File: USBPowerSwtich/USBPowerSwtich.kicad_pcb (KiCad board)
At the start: 2 copper layers, 30.8 x 17 mm, 4 parts, among them J1 USB_A_Male, J2 USB_A_Female, J3 Test, SW1 Power

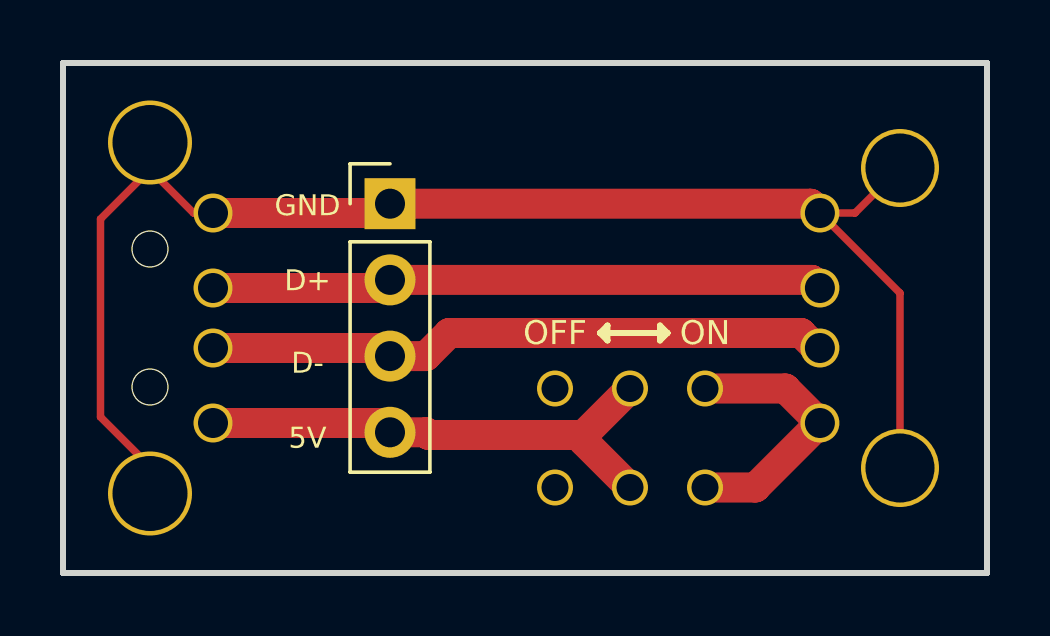
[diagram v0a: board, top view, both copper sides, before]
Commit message: Updating silkscreen and outline
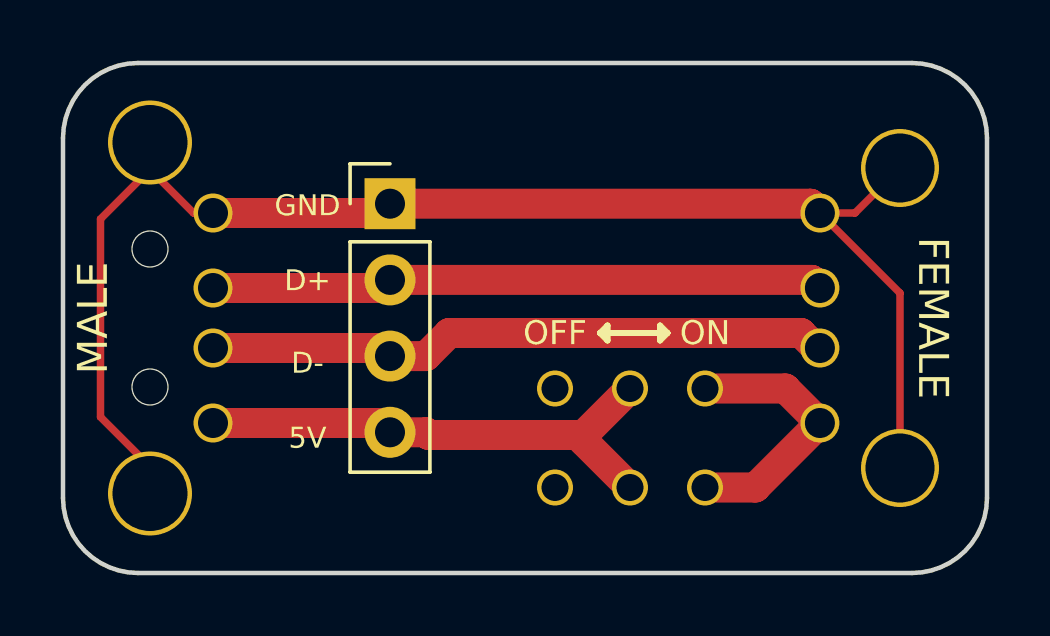
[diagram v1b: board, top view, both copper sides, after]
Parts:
- added G***: LOGO, Logos:logo_MLlabs_small, B.Cu at (87.2, 76.5)
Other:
- outline, holes or cut-outs redrawn
- board text added: "FEMALE"
- board text added: "MALE"
- board text added: "Maniacal Labs"

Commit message: Added name
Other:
- board text added: "USB Switch Buddy"
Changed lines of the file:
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@@
   (general
     (thickness 1.6)
-    (drawings 29)
+    (drawings 30)
     (tracks 38)
     (zones 0)
@@
       (xy 0.280132 4.064859)) (layer B.SilkS) (width 0.01))
   )
+  (gr_text "USB Switch Buddy" (at 78.6 87.3) (layer B.SilkS)
+    (effects (font (size 0.9 0.9) (thickness 0.225)) (justify mirror))
+  )
   (gr_text FEMALE (at 96.1 80 270) (layer F.SilkS)

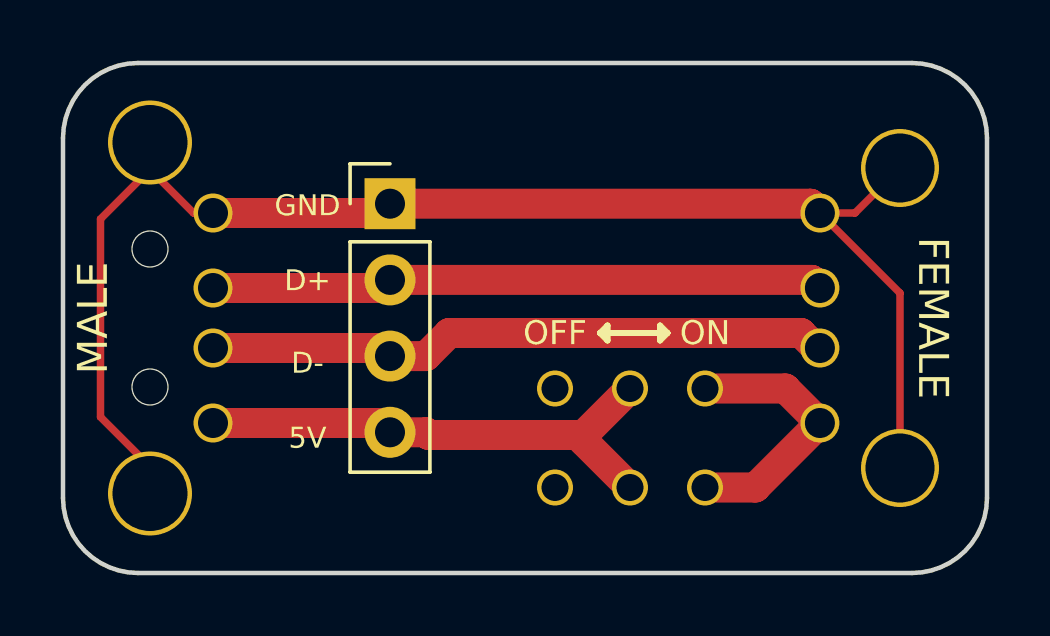
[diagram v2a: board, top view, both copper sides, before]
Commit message: Moving silk screen layout
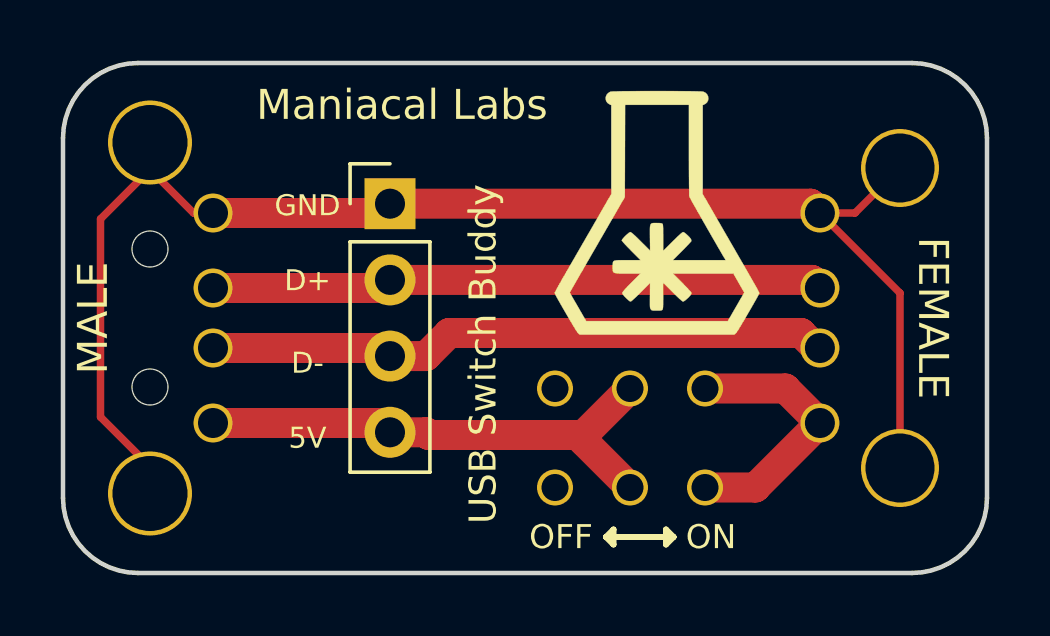
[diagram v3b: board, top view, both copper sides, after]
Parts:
- G***: moved to F.Cu
- moved G*** 0.35 mm to (86.9, 76.5), turned to 0 degrees

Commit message: Tweak switch placement
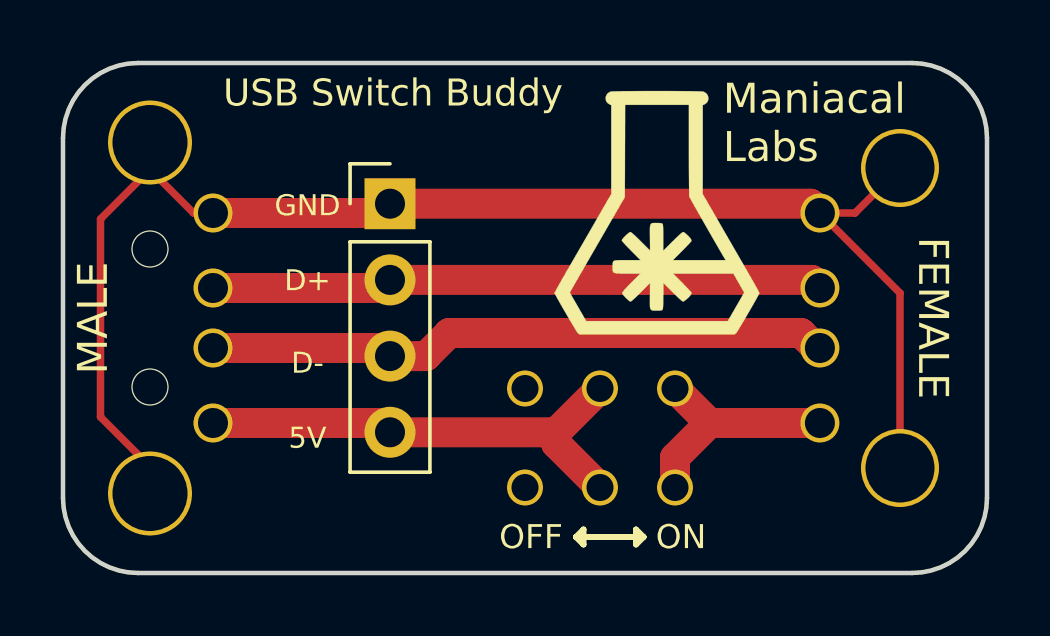
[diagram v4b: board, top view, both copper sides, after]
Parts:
- moved SW1 1.00 mm to (85.0, 84.0)
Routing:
- net Net-(J2-Pad1): track 9.03 -> 7.93 mm
- net VCC: track 17.1 -> 16.1 mm
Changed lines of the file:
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@@
     (thickness 1.6)
     (drawings 30)
-    (tracks 38)
+    (tracks 36)
     (zones 0)
     (modules 5)
@@
     (45 Margin user)
     (46 B.CrtYd user)
-    (47 F.CrtYd user)
+    (47 F.CrtYd user hide)
     (48 B.Fab user)
     (49 F.Fab user)
   )
   (setup
-    (last_trace_width 0.25)
+    (last_trace_width 1)
     (user_trace_width 1)
     (trace_clearance 0.2)
@@
     (aux_axis_origin 0 0)
     (grid_origin 67.1 88.5)
-    (visible_elements 7FFFFF7F)
+    (visible_elements 7FFFF77F)
     (pcbplotparams
       (layerselection 0x010fc_ffffffff)
@@
       (outputformat 1)
       (mirror false)
-      (drillshape 1)
+      (drillshape 0)
       (scaleselection 1)
-      (outputdirectory ""))
+      (outputdirectory "gerber/"))
   )
   (net 0 "")
@@
   )
   (module Custom:JS202011CQN (layer F.Cu)
-    (at 86 84)
+    (at 85 84)
     (descr https://www.mouser.com/datasheet/2/60/js-1382693.pdf)
     (fp_text reference SW1 (at 0 5) (layer F.SilkS) hide
@@
       (xy 0.280132 -4.064859)) (layer F.SilkS) (width 0.01))
   )
-  (gr_text "USB Switch Buddy" (at 81.1 81.2 90) (layer F.SilkS)
+  (gr_text "USB Switch Buddy" (at 78.1 72.5) (layer F.SilkS)
     (effects (font (size 0.9 0.9) (thickness 0.225)))
   )
@@
   (gr_arc (start 95.4 74) (end 97.9 74) (angle -90) (layer Edge.Cuts) (width 0.15))
   (gr_arc (start 69.6 74) (end 69.6 71.5) (angle -90) (layer Edge.Cuts) (width 0.15))
-  (gr_text "Maniacal Labs" (at 78.4 72.9) (layer F.SilkS)
-    (effects (font (size 1 1) (thickness 0.25)))
+  (gr_text "Maniacal\nLabs" (at 89.1 73.5) (layer F.SilkS)
+    (effects (font (size 1 1) (thickness 0.25)) (justify left))
   )
   (gr_text 5V (at 81 84) (layer B.SilkS)
@@
     (effects (font (size 0.7 0.7) (thickness 0.175)))
   )
-  (gr_line (start 85.45 87.55) (end 85.2 87.3) (layer F.SilkS) (width 0.2))
-  (gr_line (start 85.45 87.05) (end 85.45 87.55) (layer F.SilkS) (width 0.2))
-  (gr_line (start 85.2 87.3) (end 85.45 87.05) (layer F.SilkS) (width 0.2))
-  (gr_line (start 86.2 87.3) (end 85.2 87.3) (layer F.SilkS) (width 0.2))
-  (gr_line (start 87.2 87.55) (end 87.45 87.3) (layer F.SilkS) (width 0.2))
-  (gr_line (start 87.2 87.05) (end 87.2 87.55) (layer F.SilkS) (width 0.2))
-  (gr_line (start 87.45 87.3) (end 87.2 87.05) (layer F.SilkS) (width 0.2))
-  (gr_line (start 86.2 87.3) (end 87.45 87.3) (layer F.SilkS) (width 0.2))
-  (gr_text OFF (at 83.7 87.3) (layer F.SilkS)
+  (gr_line (start 84.45 87.55) (end 84.2 87.3) (layer F.SilkS) (width 0.2))
+  (gr_line (start 84.45 87.05) (end 84.45 87.55) (layer F.SilkS) (width 0.2))
+  (gr_line (start 84.2 87.3) (end 84.45 87.05) (layer F.SilkS) (width 0.2))
+  (gr_line (start 85.2 87.3) (end 84.2 87.3) (layer F.SilkS) (width 0.2))
+  (gr_line (start 86.2 87.55) (end 86.45 87.3) (layer F.SilkS) (width 0.2))
+  (gr_line (start 86.2 87.05) (end 86.2 87.55) (layer F.SilkS) (width 0.2))
+  (gr_line (start 86.45 87.3) (end 86.2 87.05) (layer F.SilkS) (width 0.2))
+  (gr_line (start 85.2 87.3) (end 86.45 87.3) (layer F.SilkS) (width 0.2))
+  (gr_text OFF (at 82.7 87.3) (layer F.SilkS)
     (effects (font (size 0.8 0.8) (thickness 0.2)))
   )
-  (gr_text ON (at 88.7 87.3) (layer F.SilkS)
+  (gr_text ON (at 87.7 87.3) (layer F.SilkS)
     (effects (font (size 0.8 0.8) (thickness 0.2)))
   )
@@
   (segment (start 77.69 83.5) (end 78 83.81) (width 1) (layer F.Cu) (net 2))
   (segment (start 72.1 83.5) (end 77.69 83.5) (width 1) (layer F.Cu) (net 2))
-  (segment (start 79.202081 83.81) (end 79.292081 83.9) (width 1) (layer F.Cu) (net 2))
-  (segment (start 78 83.81) (end 79.202081 83.81) (width 1) (layer F.Cu) (net 2))
-  (segment (start 84.45 83.9) (end 86 82.35) (width 1) (layer F.Cu) (net 2))
-  (segment (start 79.292081 83.9) (end 84.45 83.9) (width 1) (layer F.Cu) (net 2))
-  (segment (start 84.45 84.1) (end 86 85.65) (width 1) (layer F.Cu) (net 2))
-  (segment (start 84.45 83.9) (end 84.45 84.1) (width 1) (layer F.Cu) (net 2))
+  (segment (start 83.54 83.81) (end 85 82.35) (width 1) (layer F.Cu) (net 2))
+  (segment (start 78 83.81) (end 83.54 83.81) (width 1) (layer F.Cu) (net 2))
+  (segment (start 83.54 84.19) (end 85 85.65) (width 1) (layer F.Cu) (net 2))
+  (segment (start 83.54 83.81) (end 83.54 84.19) (width 1) (layer F.Cu) (net 2))
   (segment (start 77.73 81) (end 78 81.27) (width 1) (layer F.Cu) (net 3))
   (segment (start 72.1 81) (end 77.73 81) (width 1) (layer F.Cu) (net 3))
@@
   (segment (start 92.06 78.73) (end 92.33 79) (width 1) (layer F.Cu) (net 4))
   (segment (start 78 78.73) (end 92.06 78.73) (width 1) (layer F.Cu) (net 4))
-  (segment (start 91.18 82.35) (end 92.33 83.5) (width 1) (layer F.Cu) (net 5))
-  (segment (start 88.5 82.35) (end 91.18 82.35) (width 1) (layer F.Cu) (net 5))
-  (segment (start 90.18 85.65) (end 92.33 83.5) (width 1) (layer F.Cu) (net 5))
-  (segment (start 88.5 85.65) (end 90.18 85.65) (width 1) (layer F.Cu) (net 5))
+  (segment (start 87.5 82.35) (end 88.65 83.5) (width 1) (layer F.Cu) (net 5))
+  (segment (start 88.65 83.5) (end 92.33 83.5) (width 1) (layer F.Cu) (net 5))
+  (segment (start 87.5 84.65) (end 88.65 83.5) (width 1) (layer F.Cu) (net 5))
+  (segment (start 87.5 85.65) (end 87.5 84.65) (width 1) (layer F.Cu) (net 5))
 )
